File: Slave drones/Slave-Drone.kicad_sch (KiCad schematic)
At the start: 39 parts

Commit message: Completely routed the PCB
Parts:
- removed D? (x4): 1N4007, Diode_THT:D_DO-41_SOD81_P10.16mm_Horizontal, symbol Diode:1N4007
- added C3: 10uF, Capacitor_SMD:C_0603_1608Metric, symbol Device:C
- added D1, D2, D3, D4: SS14, Diode_SMD:D_SMA, symbol Diode:SS14
- added D6: MBRA340, Diode_SMD:D_SMA, symbol Diode:MBRA340
- C1: renamed from C?; footprint (none) -> Capacitor_SMD:C_0402_1005Metric
- C2: renamed from R?; footprint (none) -> Capacitor_SMD:C_0603_1608Metric; symbol Device:R -> Device:C
- J1, J2, J3, J4, J6: renamed from J?; footprint (none) -> Connector_PinHeader_2.54mm:PinHeader_1x02_P2.54mm_Vertical
- J5: renamed from J?; footprint (none) -> Connector_USB:USB_C_Receptacle_HCTL_HC-TYPE-C-16P-01A
- MOSFET1, MOSFET2, MOSFET3, MOSFET4: renamed from MOSFET?; footprint SOT-23_MCC -> SI2302:SOT-23_MCC
- R1, R10, R11, R12, R16, R17, R2, R3, R4, R5, R6, R7, R8, R9: renamed from R?; footprint (none) -> Resistor_SMD:R_0402_1005Metric
- R13, R14: renamed from R?; footprint (none) -> Resistor_SMD:R_0402_1005Metric_Pad0.72x0.64mm_HandSolder
- SW1, SW2: renamed from SW?; footprint (none) -> Button_Switch_SMD:SW_Push_SPST_NO_Alps_SKRK
- U1: renamed from U?; footprint footprint:QFN-24_L3.0-W3.0-P0.40-BL-EP -> footprint-JLC:QFN-24_L3.0-W3.0-P0.40-BL-EP
- U2: renamed from U?; footprint footprint:LGA-16_L3.0-W3.0-P0.50-BL_SQ -> footprint-JLC:LGA-16_L3.0-W3.0-P0.50-BL_SQ
- U3: renamed from U?; footprint RF_Module:ESP32-S2-MINI-1 -> footprint-JLC:BULETM-SMD_ESP32-S3-MINI-1-N8
- gave numbers to parts that had none: 2
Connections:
- net GND: now also C3.2
- net Motor_Power: now also D1.1 (K), D2.1 (K), D3.1 (K), D4.1 (K), D6.2 (A); no longer D5.1 (K), U4.1 (VIN)
- net at J2.2 (Pin_2), MOSFET2.3 (D): now also D2.2 (A)
- net at J3.2 (Pin_2), MOSFET3.3 (D): now also D3.2 (A)
- net at J1.2 (Pin_2), MOSFET1.3 (D): now also D1.2 (A)
- net at J4.2 (Pin_2), MOSFET4.3 (D): now also D4.2 (A)
- net USBPWR: now reaches U4.3 (EN)
- net USBPWR: now also D5.1 (K), U4.1 (VIN), C3.1, D6.1 (K)
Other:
- moved on the sheet: J6

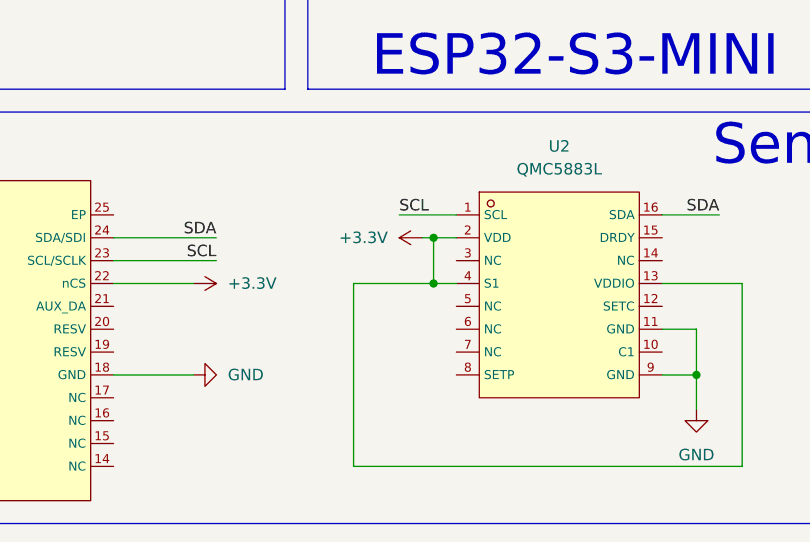
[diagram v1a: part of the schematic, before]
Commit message: changed QMC5338L to QMC5338P
Has the same symbol/footprint but slightly different wiring
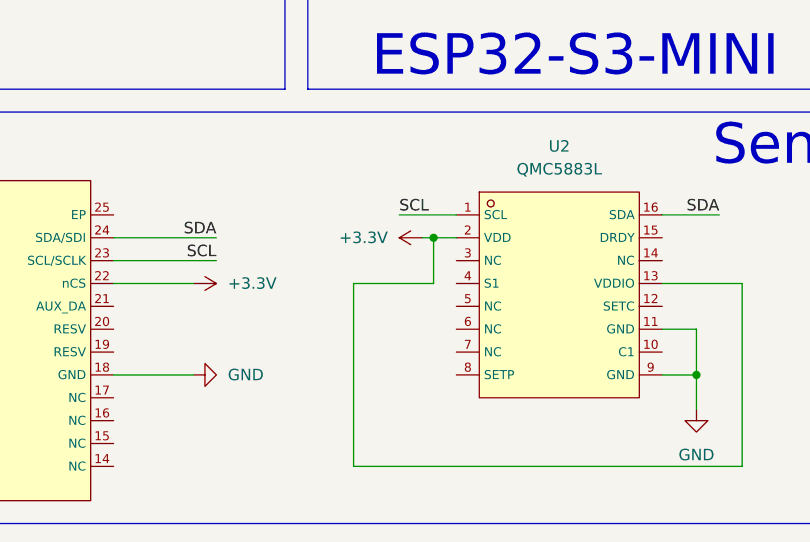
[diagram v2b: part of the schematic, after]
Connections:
- net +3.3V: no longer U2.4 (S1)

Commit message: updated QMC5883P/MPU6500/ESP32 footprints
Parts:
- U1: footprint footprint-JLC:QFN-24_L3.0-W3.0-P0.40-BL-EP -> Sensor_Motion:InvenSense_QFN-24_3x3mm_P0.4mm
- U2: footprint footprint-JLC:LGA-16_L3.0-W3.0-P0.50-BL_SQ -> footprints-QMC:QMC5883L_QST
- U3: footprint footprint-JLC:BULETM-SMD_ESP32-S3-MINI-1-N8 -> esp32:XCVR_ESP32-S3-MINI-1-N8
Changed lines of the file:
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@@
 			)
 		)
-		(property "Footprint" "footprint-JLC:QFN-24_L3.0-W3.0-P0.40-BL-EP"
+		(property "Footprint" "Sensor_Motion:InvenSense_QFN-24_3x3mm_P0.4mm"
 			(at 50.8 186.69 0)
 			(hide yes)
@@
 			)
 		)
-		(property "Footprint" "footprint-JLC:LGA-16_L3.0-W3.0-P0.50-BL_SQ"
+		(property "Footprint" "footprints-QMC:QMC5883L_QST"
 			(at 118.11 181.61 0)
 			(hide yes)
@@
 			)
 		)
-		(property "Footprint" "footprint-JLC:BULETM-SMD_ESP32-S3-MINI-1-N8"
+		(property "Footprint" "esp32:XCVR_ESP32-S3-MINI-1-N8"
 			(at 167.64 119.38 0)
 			(hide yes)
